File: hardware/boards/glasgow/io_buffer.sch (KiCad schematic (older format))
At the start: 65 parts, among them J2 Conn_02x10_Odd_Even, J6 Conn_01x08, J7 Conn_01x08, U10 DAC081C081CIMK, U11 TPS73101DBV, U16 SN74LVC1T45DRL, U17 SN74LVC1T45DRL, U18 SN74LVC1T45DRL, U19 PCA6408APW, U19 SN74LVC1T45DRL, U20 SN74LVC1T45DRL, U21 INA233, U21 SN74LVC1T45DRL, U5 SN74LVC1T45DRL, U6 SN74LVC1T45DRL

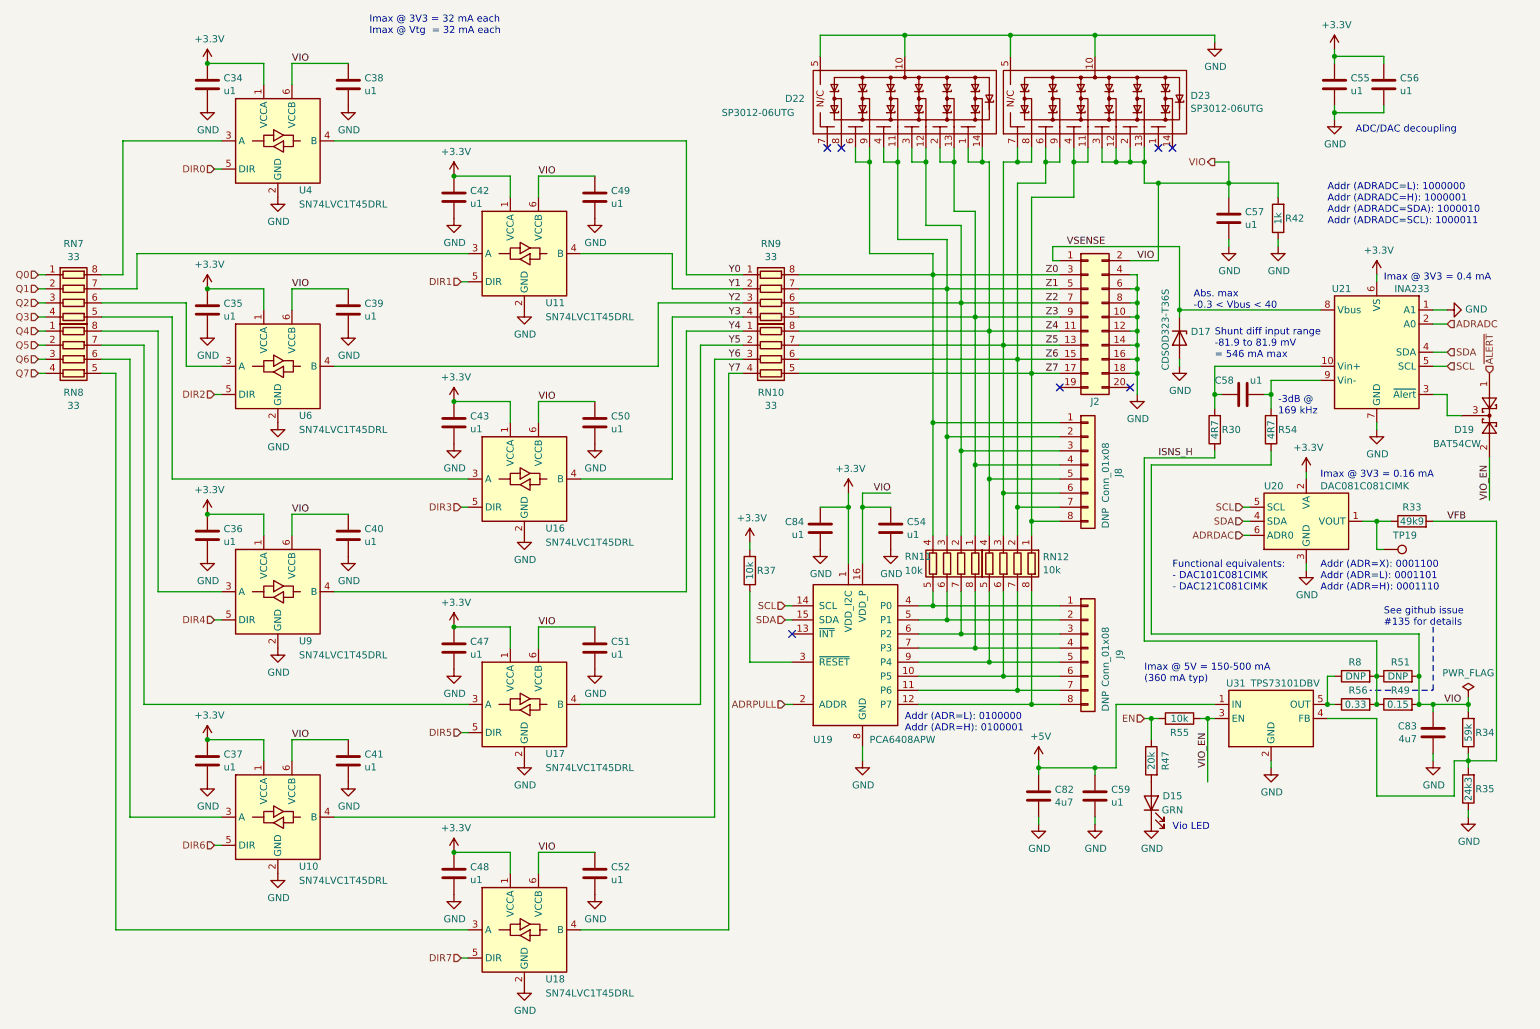
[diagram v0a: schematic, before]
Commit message: revC2: save one BOM line by replacing 1k resistors with 2k2
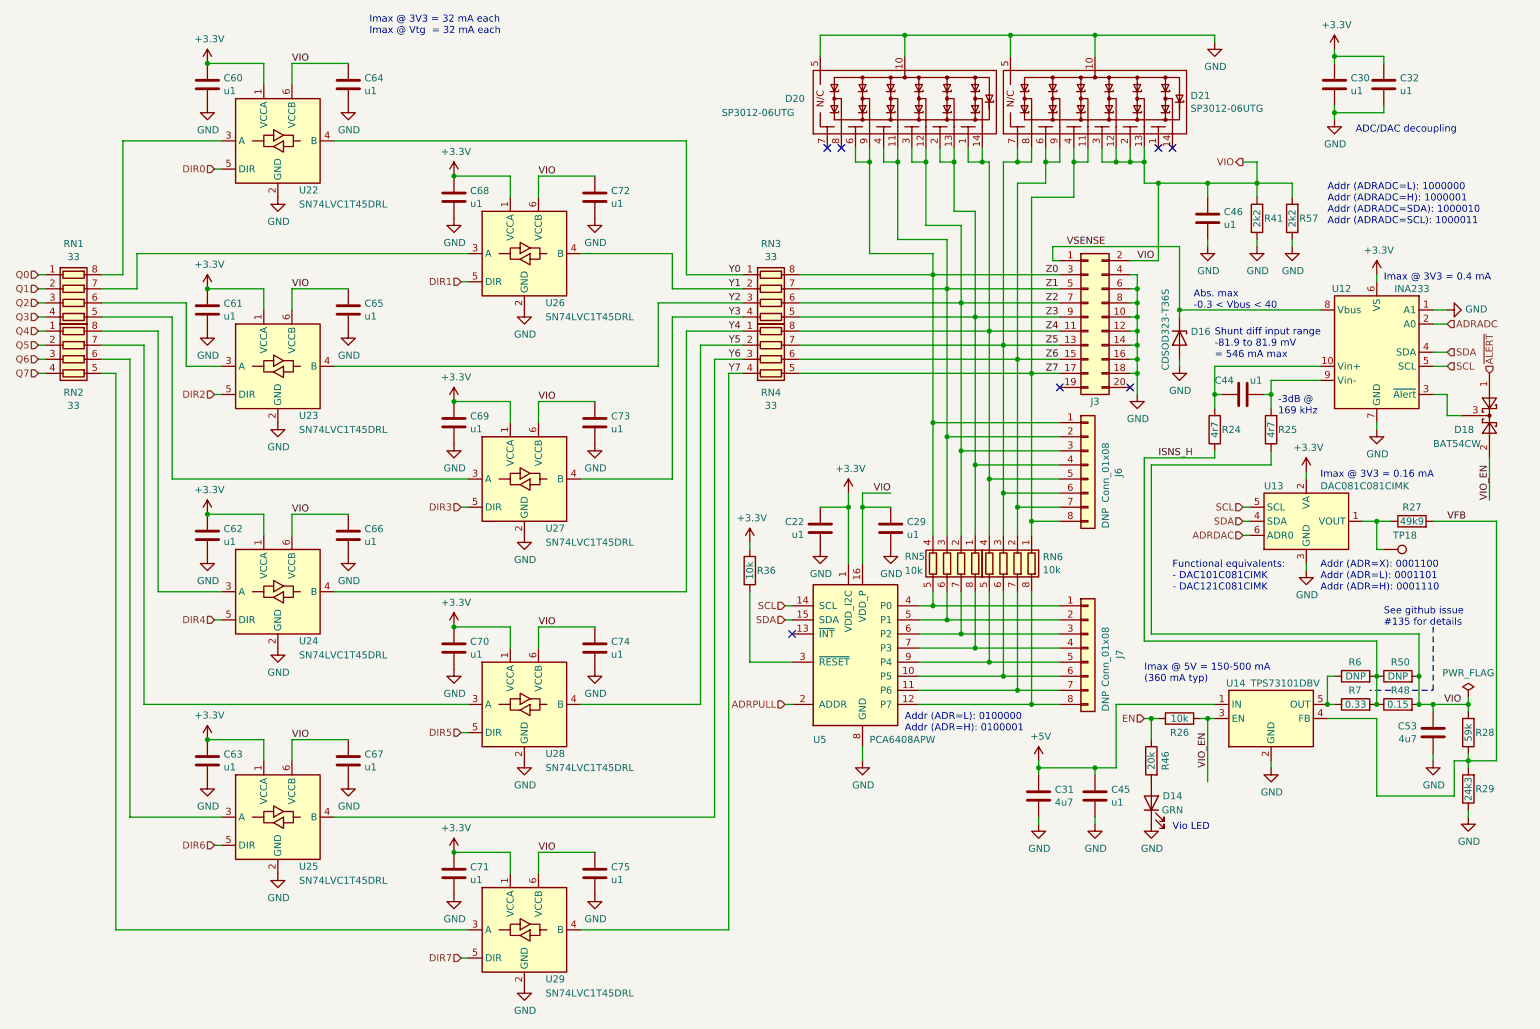
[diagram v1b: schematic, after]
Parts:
- added R58: 2k2, Resistor_SMD:R_0402_1005Metric, symbol Device:R
- R30, R54: value 4R7 -> 4r7
- R42: value 1k -> 2k2; 1b2-bom-key res-0402-1k -> res-0402-2k2; MPN RC0402FR-131KL -> RC0402FR-132K2L
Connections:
- net GND: now also R58.1
- net VIO: now also R58.2
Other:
- moved on the sheet: C46, R41

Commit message: revC2: Switched bulk cap footprint, Added system reset button circuit.
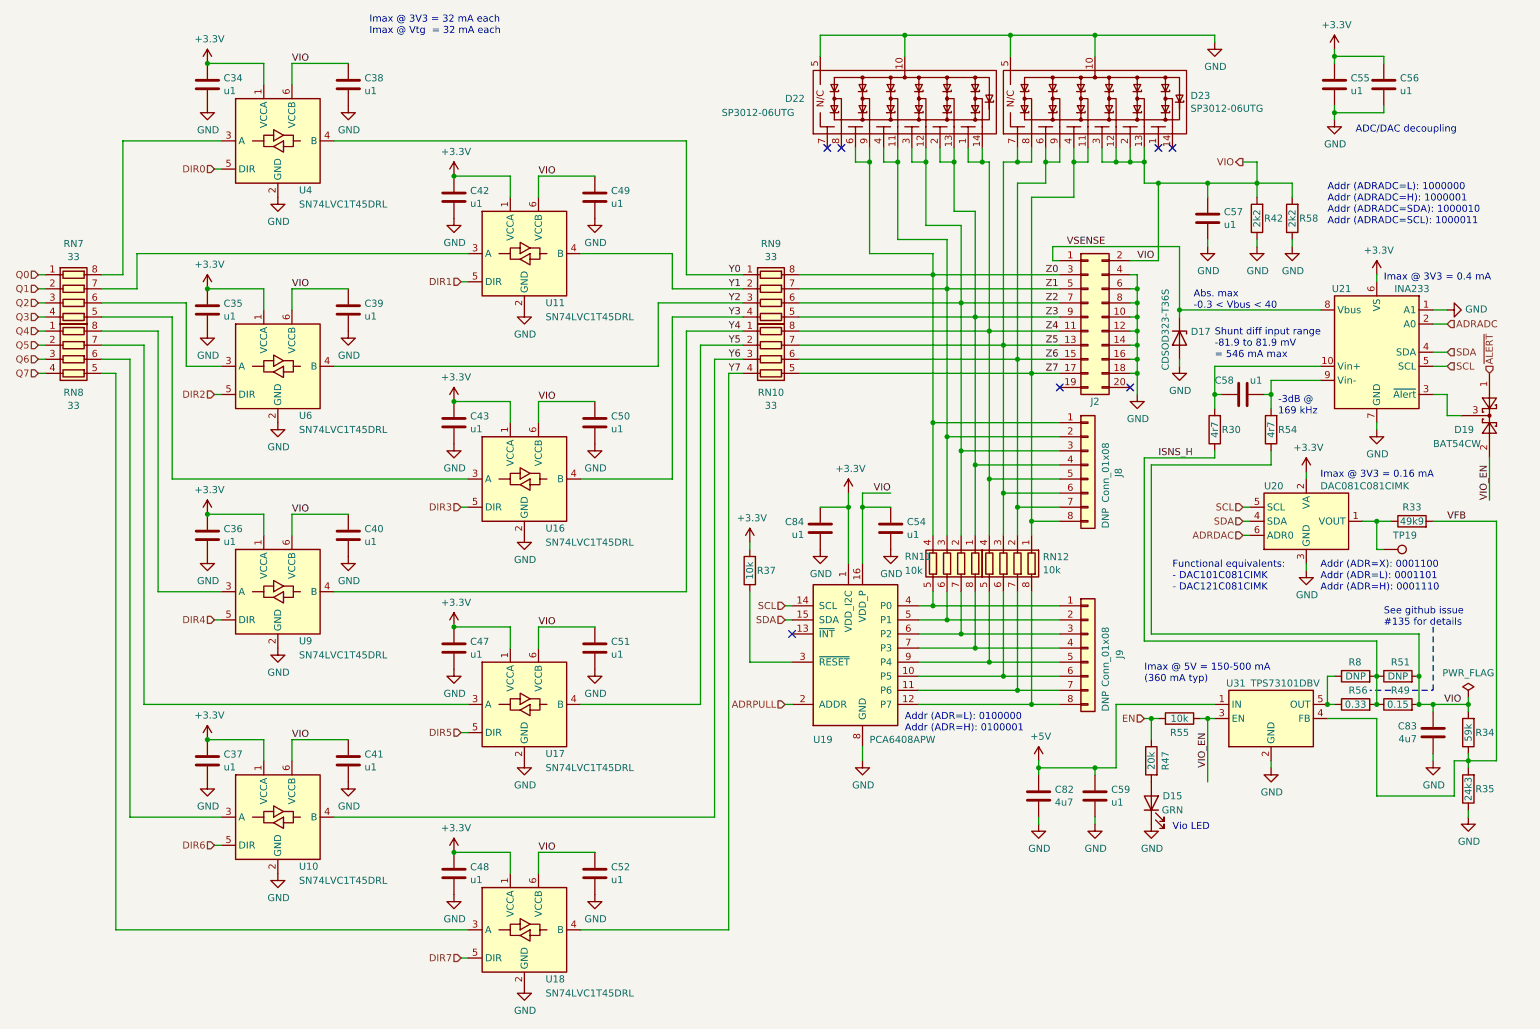
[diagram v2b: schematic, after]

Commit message: revC2: Replaced 0603 HandSolder footprints with regular ones.
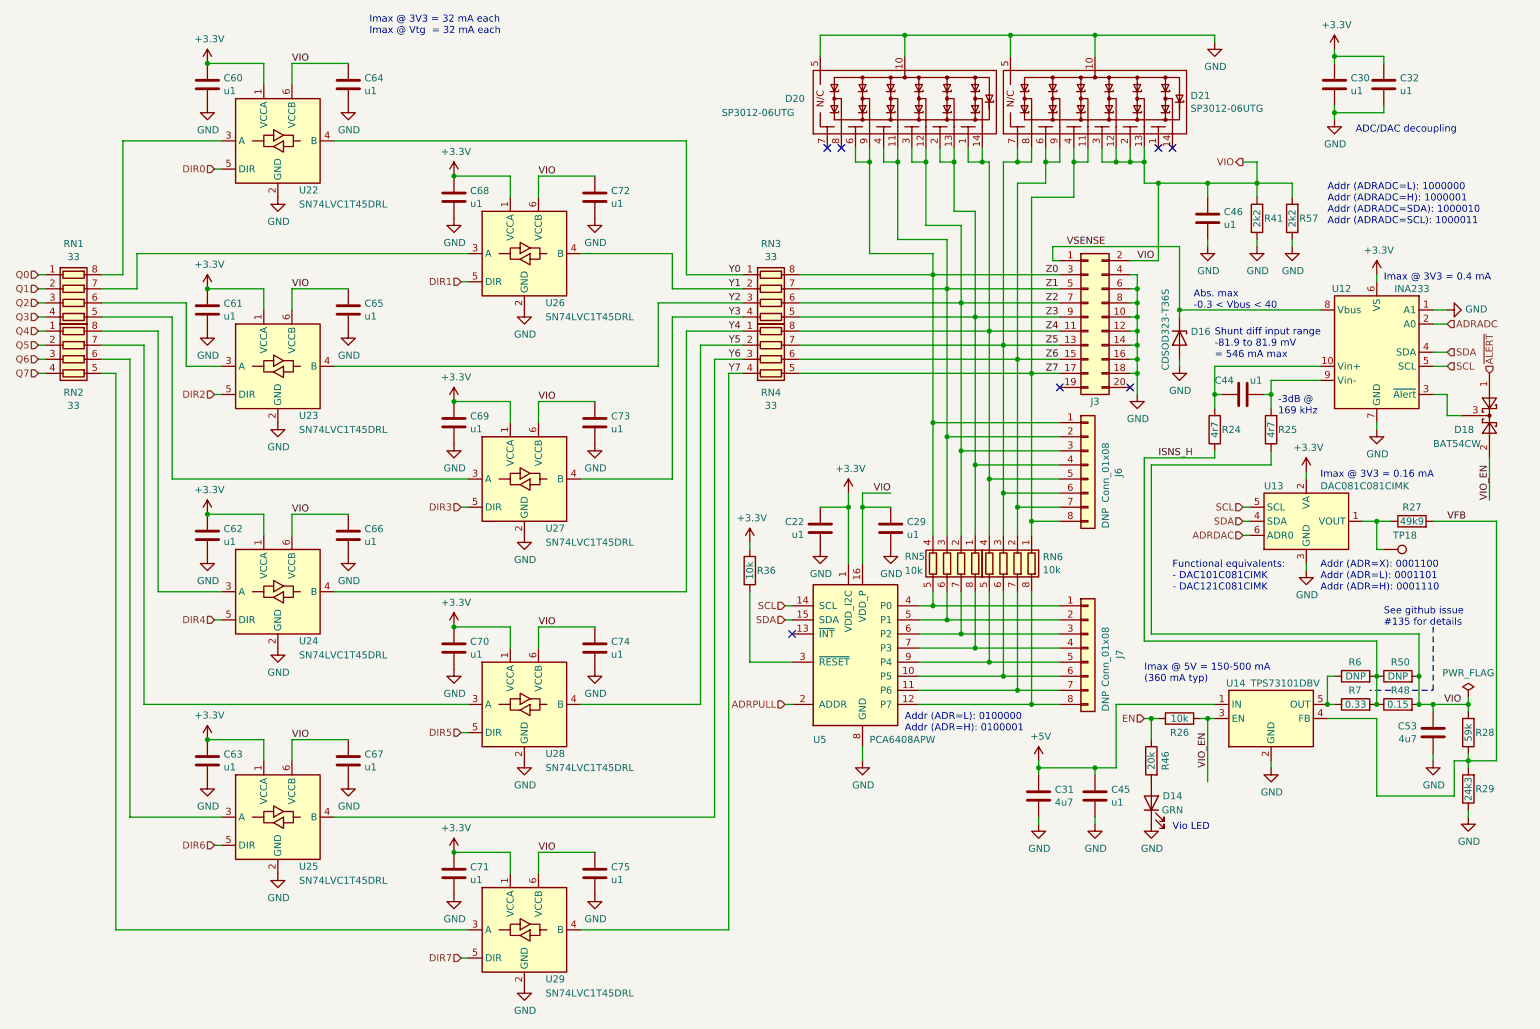
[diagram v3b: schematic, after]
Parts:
- C82, C83: footprint Capacitor_SMD:C_0603_1608Metric_Pad1.05x0.95mm_HandSolder -> Capacitor_SMD:C_0603_1608Metric
- D14: footprint LED_SMD:LED_0603_1608Metric_Pad1.05x0.95mm_HandSolder -> LED_SMD:LED_0603_1608Metric

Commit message: revC2: Replaced top actuated tact switch with a side actuated one.
This should make the case design better. This is not necessarily the
final tact switch selection.
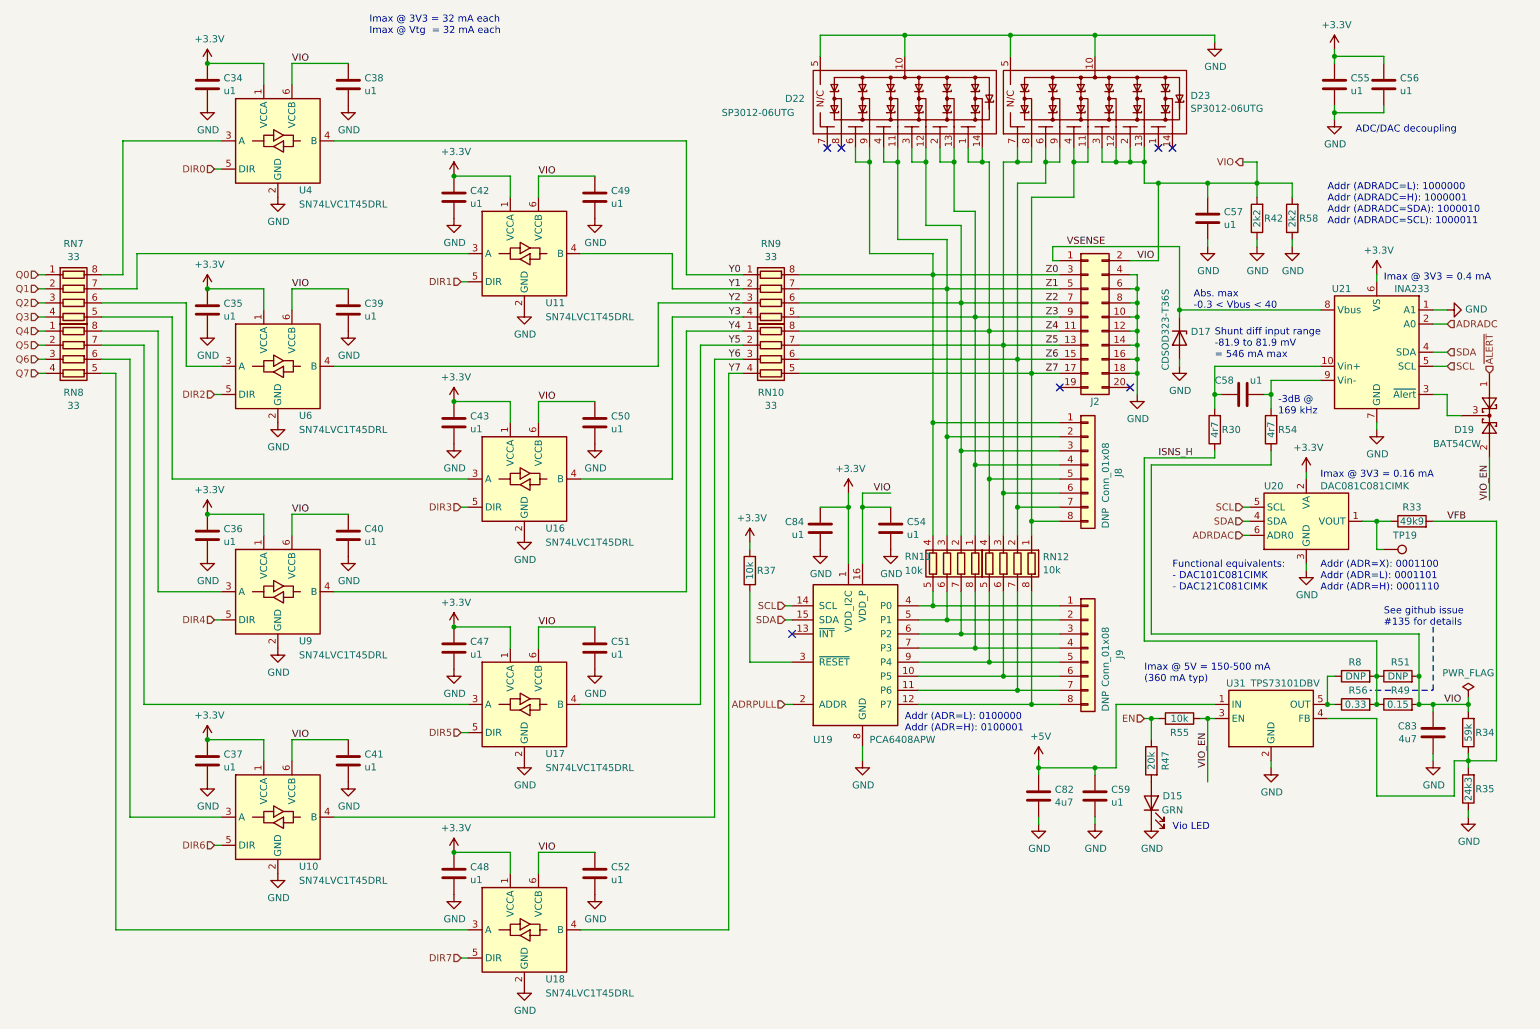
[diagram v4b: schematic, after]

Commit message: revC2: Updated 1b2-bom-keys and corrected levelshifter PN.
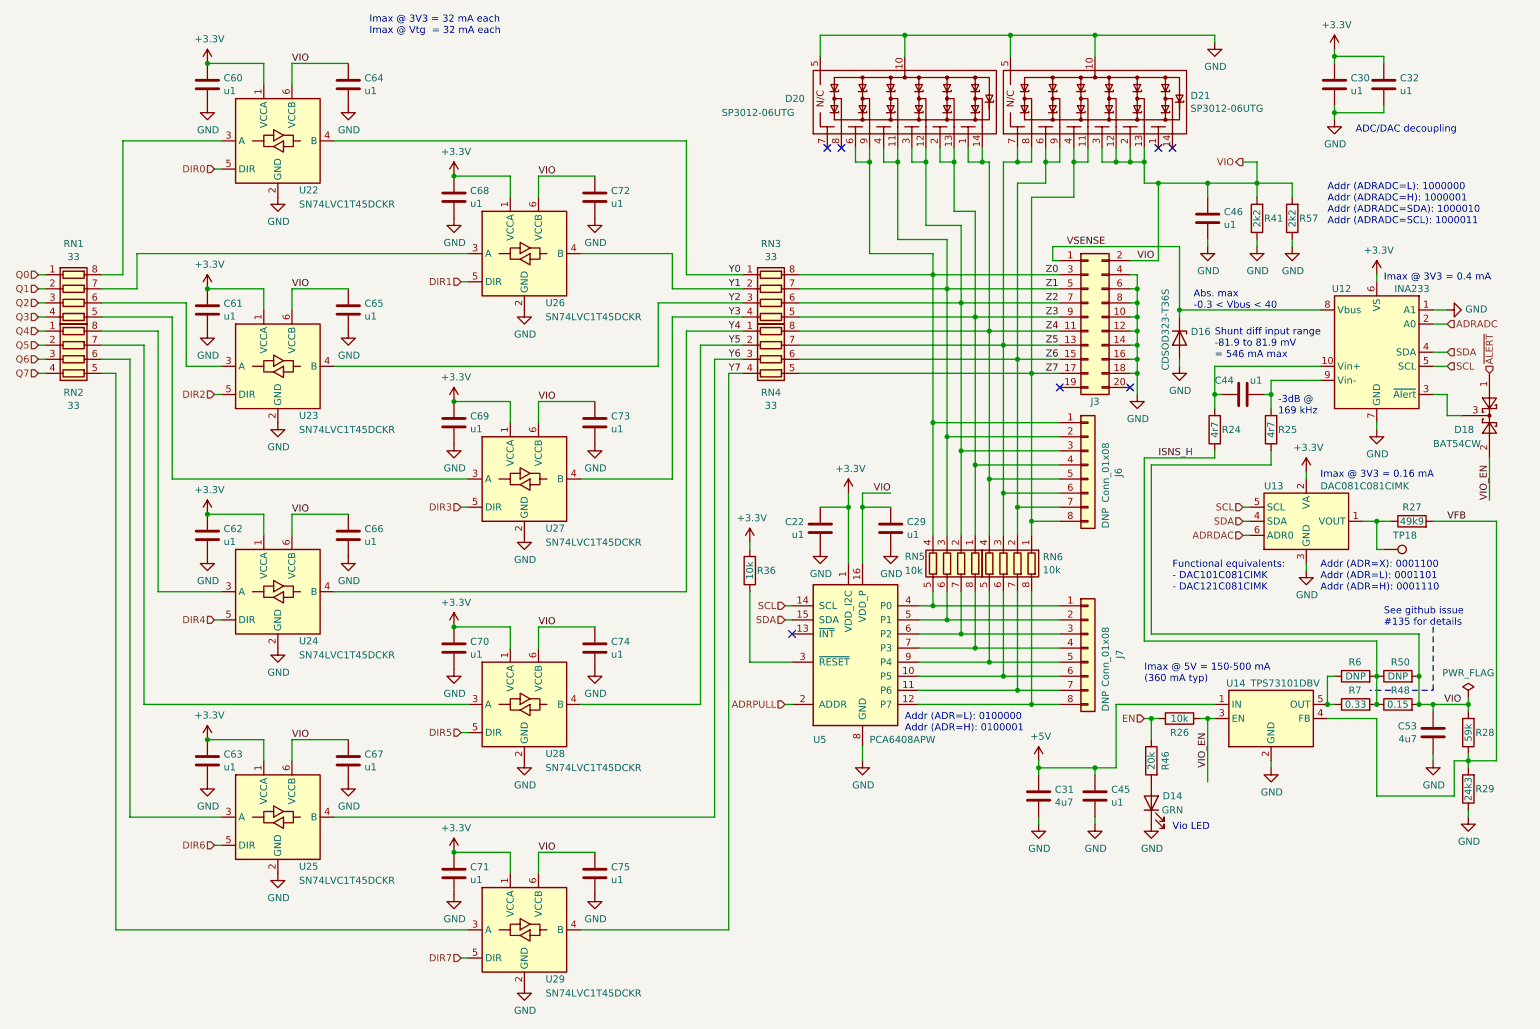
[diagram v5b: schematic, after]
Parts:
- D17: 1b2-bom-key (none) -> esd-diode-sod323-cdsod323-t36s
- D19: 1b2-bom-key (none) -> diode-sot323-bat54cw
- D22, D23: 1b2-bom-key (none) -> diode-14udfn-sp3012-06utg
- RN1, RN2, RN3, RN4: 1b2-bom-key (none) -> res-0402cv-array-4-33
- RN5, RN6: 1b2-bom-key (none) -> res-0402cv-array-4-10k
- U16, U17, U18, U19, U20, U21, U5, U6: value SN74LVC1T45DRL -> SN74LVC1T45DCKR; 1b2-bom-key ic-sot563-sn74lvc1t45drl -> ic-sot563-sn4lvc1t45dckr
- U21: 1b2-bom-key (none) -> ic-vssop10-ina233
